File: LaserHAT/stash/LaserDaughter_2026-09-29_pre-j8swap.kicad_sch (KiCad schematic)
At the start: 29 parts, among them J1 HAT_J8, J2 Conn_02x02_Counter_Clockwise, J3 HAT_J9, J4 PD_K-LASER_V (solder jumper), J5 RED_SHUNT, Q1 SI3134KDWA-TP, Q2 NDT3055L, SW5 SW_SPDT, U2 MT3608, U3 TLV2371DBV

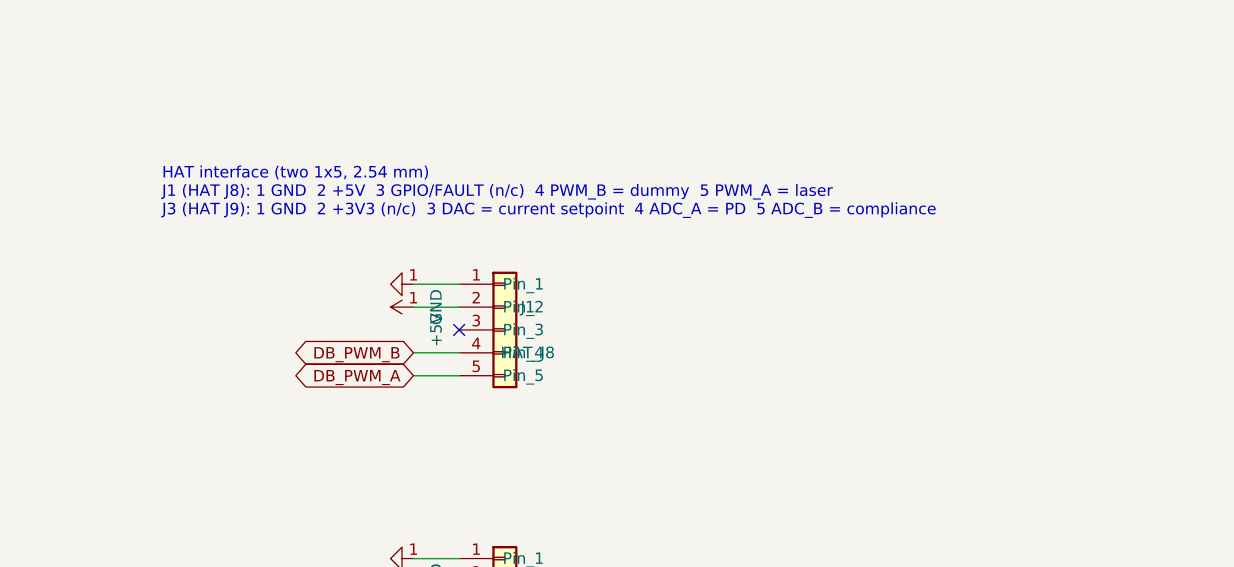
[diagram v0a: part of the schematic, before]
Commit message: LaserHAT: J8.3 = FAULT_n (PA6), J8.5 = EN/PWM_A (PA7) on the HAT and the laser module
Follows the e-stim module's connector standard (spec §3/§7, LAYOUT_HANDOFF Q2):
- bnc_daughter_io.kicad_sch: DB_GPIO on J8.3, DB_PWM_A on J8.5 (rev2_migrate.py matches)
- LaserDriver.kicad_pcb: J8 pads re-netted, PA6/PA7 traces re-routed along the old
  corridors (same vias at U7); DRC unchanged, 0 unconnected; backup in stash/
- LaserDaughter: J1.5 = DB_PWM_A, J1.3 n/c; schematic regenerated, board re-routed
- REV2_NOTES/CLAUDE.md: PA17/PA22 rows now say I2C SDA/SCL; note on why hardware I2C1
  cannot use them and the re-map that would (J9.4 -> PA16, J9.5 -> PA17, BUTTON3 -> PA22)
- LAYOUT_HANDOFF Q1/Q2 answered, spec §7 marked applied, fab outputs regenerated
- tools/schlib.py: symbol dir from env / Linux default

Co-Authored-By: Claude Fable 5.1 <noreply@anthropic.com>
Claude-Session: https://claude.ai/code/session_018vgLizGzYPynnY93ajvoVA
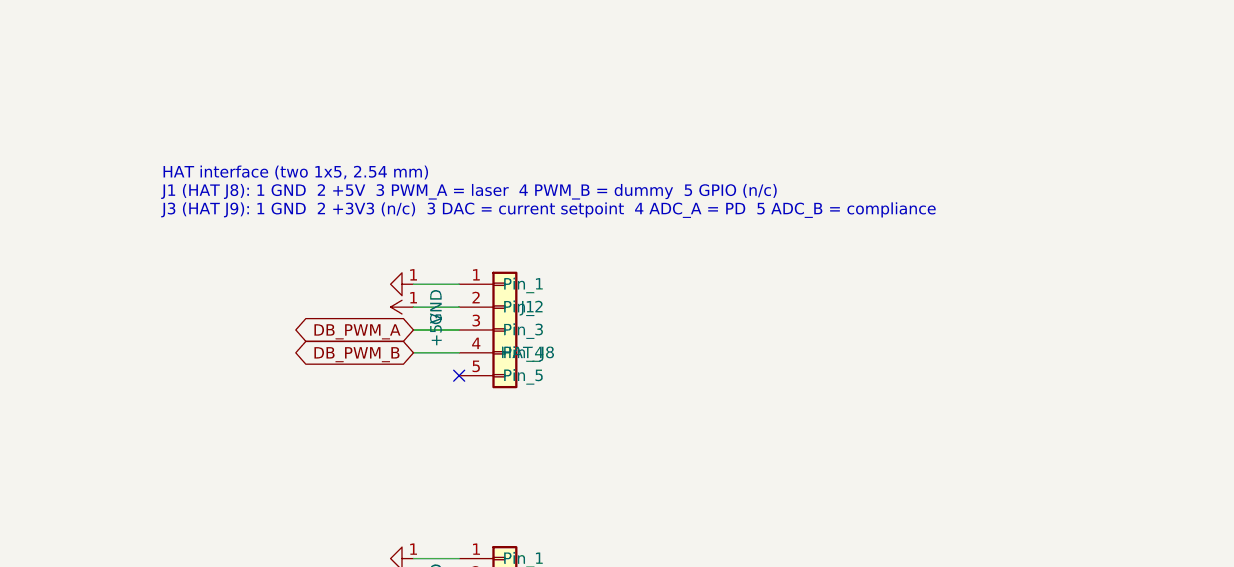
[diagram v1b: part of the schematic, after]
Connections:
- net DB_PWM_A: now also J1.3 (Pin_3); no longer J1.5 (Pin_5)
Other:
- note added: "HAT interface (two 1x5, 2.54 mm) J1 (HAT J8): 1 GND 2 +5V 3 PWM_A = laser 4 PWM_B = dummy 5 GPIO (n/c) J3 (HAT J9): 1 GND 2 +3V3 (n/c) 3 DAC = current setpoint 4 ADC_A = PD 5 ADC_B = compliance"
- note removed: "HAT interface (two 1x5, 2.54 mm) J1 (HAT J8): 1 GND 2 +5V 3 GPIO/FAULT (n/c) 4 PWM_B = dummy 5 PWM_A = laser J3 (HAT J9): 1 GND 2 +3V3 (n/c) 3 DAC = current setpoint 4 ADC_A = PD 5 ADC_B = compliance"
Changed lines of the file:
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@@
+    (stroke (width 0.0))
+  )
+  (wire (pts (xy 325.12 116.84) (xy 320.04 116.84))
     (stroke (width 0.0))
   )
   (wire (pts (xy 325.12 119.38) (xy 320.04 119.38))
-    (stroke (width 0.0))
-  )
-  (wire (pts (xy 325.12 121.92) (xy 320.04 121.92))
     (stroke (width 0.0))
   )
@@
     )
   )
+  (global_label "DB_PWM_A" (shape bidirectional) (at 320.04 116.84 180) (fields_autoplaced)
+    (effects (font (size 1.27 1.27)) (justify right))
+    (property "Intersheetrefs" "${INTERSHEET_REFS}" (id 0) (at 320.04 116.84 0)
+      (effects (font (size 1.27 1.27)) hide)
+    )
+  )
   (global_label "DB_PWM_B" (shape bidirectional) (at 320.04 119.38 180) (fields_autoplaced)
     (effects (font (size 1.27 1.27)) (justify right))
     (property "Intersheetrefs" "${INTERSHEET_REFS}" (id 0) (at 320.04 119.38 0)
-      (effects (font (size 1.27 1.27)) hide)
-    )
-  )
-  (global_label "DB_PWM_A" (shape bidirectional) (at 320.04 121.92 180) (fields_autoplaced)
-    (effects (font (size 1.27 1.27)) (justify right))
-    (property "Intersheetrefs" "${INTERSHEET_REFS}" (id 0) (at 320.04 121.92 0)
       (effects (font (size 1.27 1.27)) hide)
     )
@@
     )
   )
-  (no_connect (at 325.12 116.84))
+  (no_connect (at 325.12 121.92))
   (no_connect (at 325.12 144.78))
   (text "Current setpoint: I_LD = V(IREF) / Rs1 = DAC x (10k / 49k) / 2R  (full scale ~335 mA)\nDummy load: D3 + D2 (+ D4 unless J5 shunted). J5 ON = red LD (~2.8 V), OFF = blue LD (~5.5 V).\nQ2 dissipation: red on 5 V ~0.5 W, blue on 12 V ~0.8 W -> SOT-223 on copper.\nUse the 5 V setting for a single red LD (12 V would put ~2.5 W into Q2)."
@@
     (effects (font (size 1.27 1.27)) (justify left))
   )
-  (text "HAT interface (two 1x5, 2.54 mm)\nJ1 (HAT J8): 1 GND  2 +5V  3 GPIO/FAULT (n/c)  4 PWM_B = dummy  5 PWM_A = laser\nJ3 (HAT J9): 1 GND  2 +3V3 (n/c)  3 DAC = current setpoint  4 ADC_A = PD  5 ADC_B = compliance"
+  (text "HAT interface (two 1x5, 2.54 mm)\nJ1 (HAT J8): 1 GND  2 +5V  3 PWM_A = laser  4 PWM_B = dummy  5 GPIO (n/c)\nJ3 (HAT J9): 1 GND  2 +3V3 (n/c)  3 DAC = current setpoint  4 ADC_A = PD  5 ADC_B = compliance"
     (at 292.1 101.6 0)
     (effects (font (size 1.27 1.27)) (justify left))
